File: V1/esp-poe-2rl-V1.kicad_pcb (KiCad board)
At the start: 4 copper layers, 88 x 45 mm, 100 parts, among them J1 USB_C_Receptacle_USB2.0, J2 1x2P 5,08mm, J3 1x2P 5,08mm, J4 RJ45 JACK, K1 G5NB-1A-E-DC5, K2 G5NB-1A-E-DC5, Q1 WPM2015-3/TR, Q2 LMUN2211LT1G, Q3 UMH3N, Q4 MMBT2222A, Q5 MMBT2222A, SW1 RESET, U1 CH340K, U2 ESP32-WROOM-32UE-N16, U3 LAN8710A, U4 TX4138, U5 SY8089A1AAC, U6 TPS2376DDAR-H

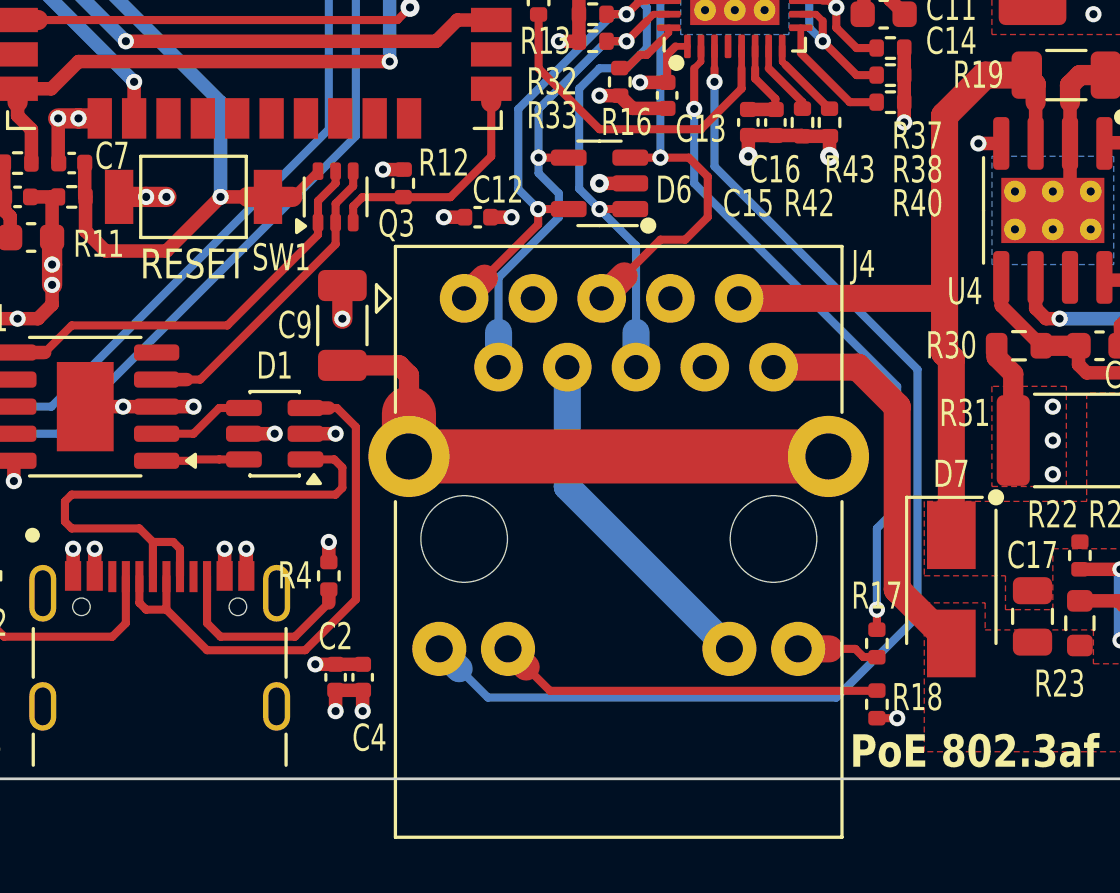
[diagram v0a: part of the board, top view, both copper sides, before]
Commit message: Update power rail names
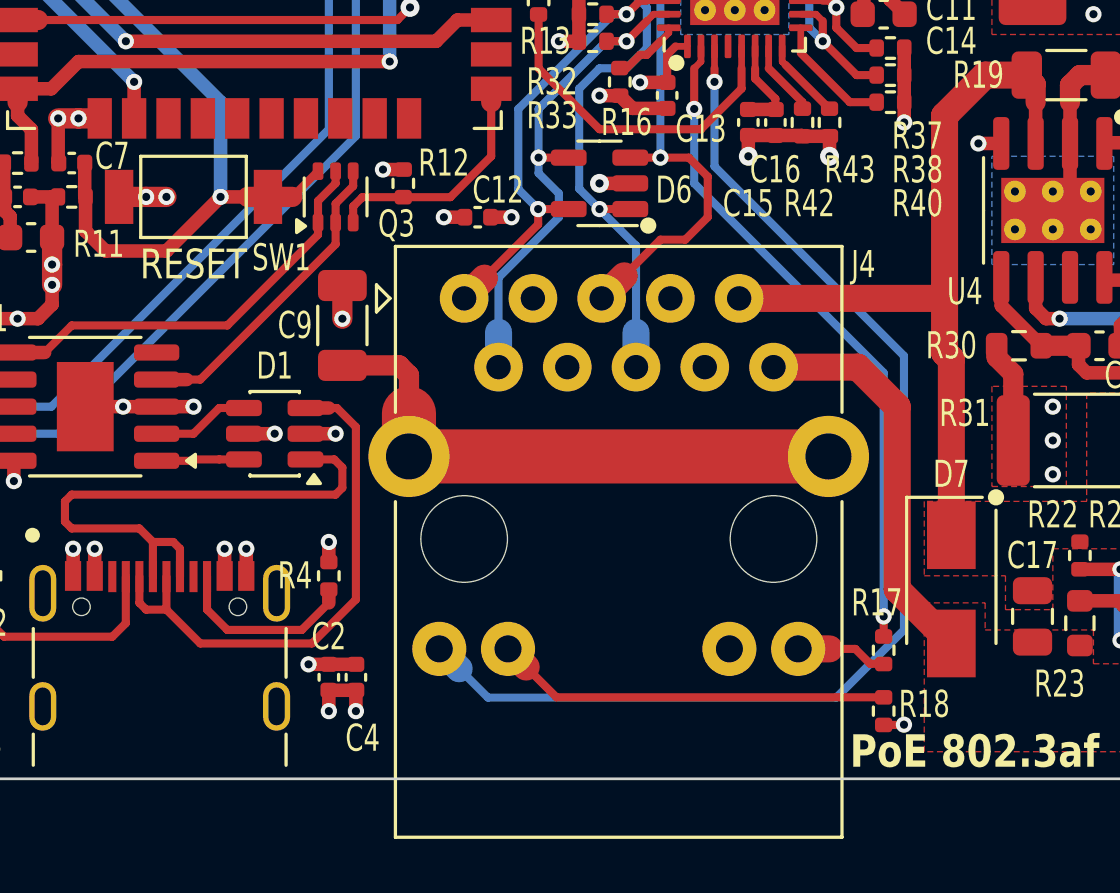
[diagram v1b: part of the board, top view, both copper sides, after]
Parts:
- moved R17 0.35 mm to (137.5, 111.2)
- moved R18 0.35 mm to (137.5, 113.5)
- moved C2 0.25 mm to (117.0, 112.2)
- moved C4 0.25 mm to (118.0, 112.2)
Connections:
- J4 pad 13: +3V3A -> +3V3LAN
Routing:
- net +3V3LAN: track 13.4 -> 36.8 mm
- net +3V3A: track 27.8 -> 14.9 mm
- net 5VUSB: track 88.9 -> 96.8 mm
- net /USBCC2: track 7.43 -> 6.93 mm

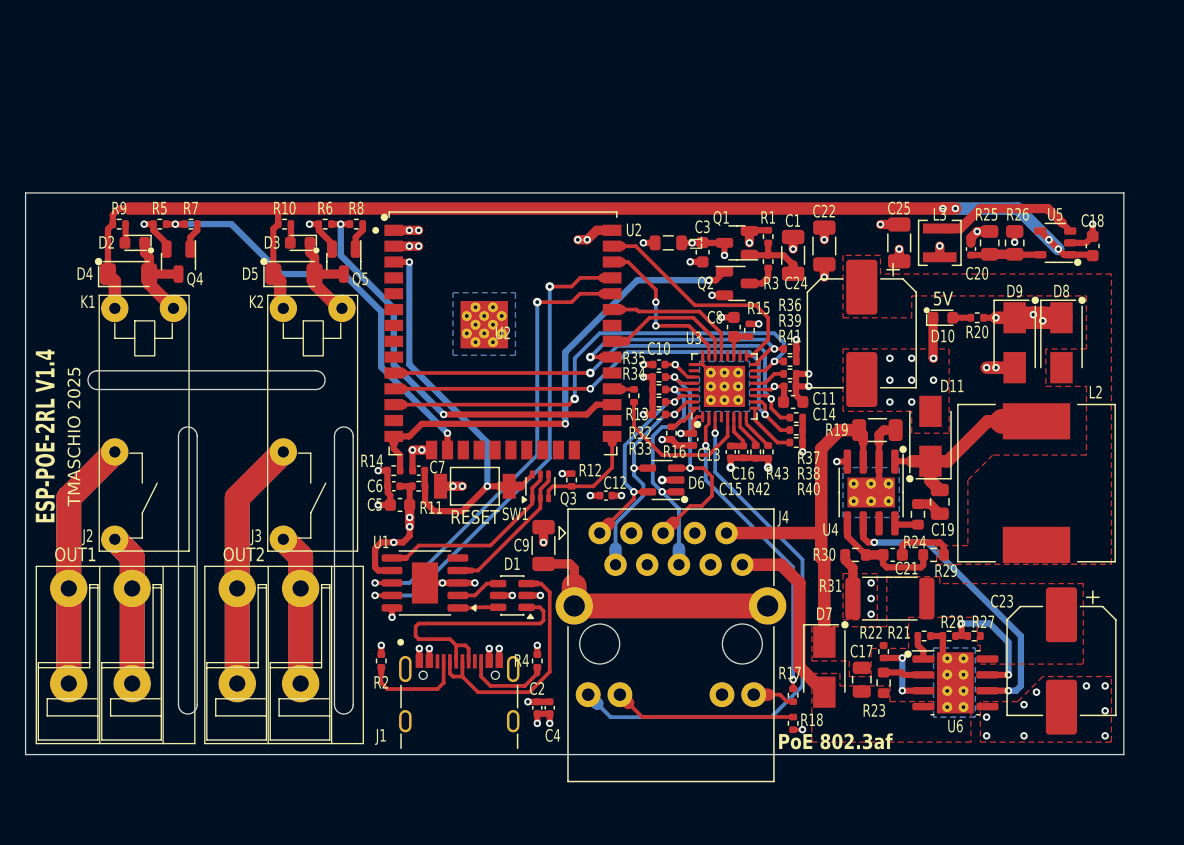
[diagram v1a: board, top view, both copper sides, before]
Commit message: addressing the PHY power rails
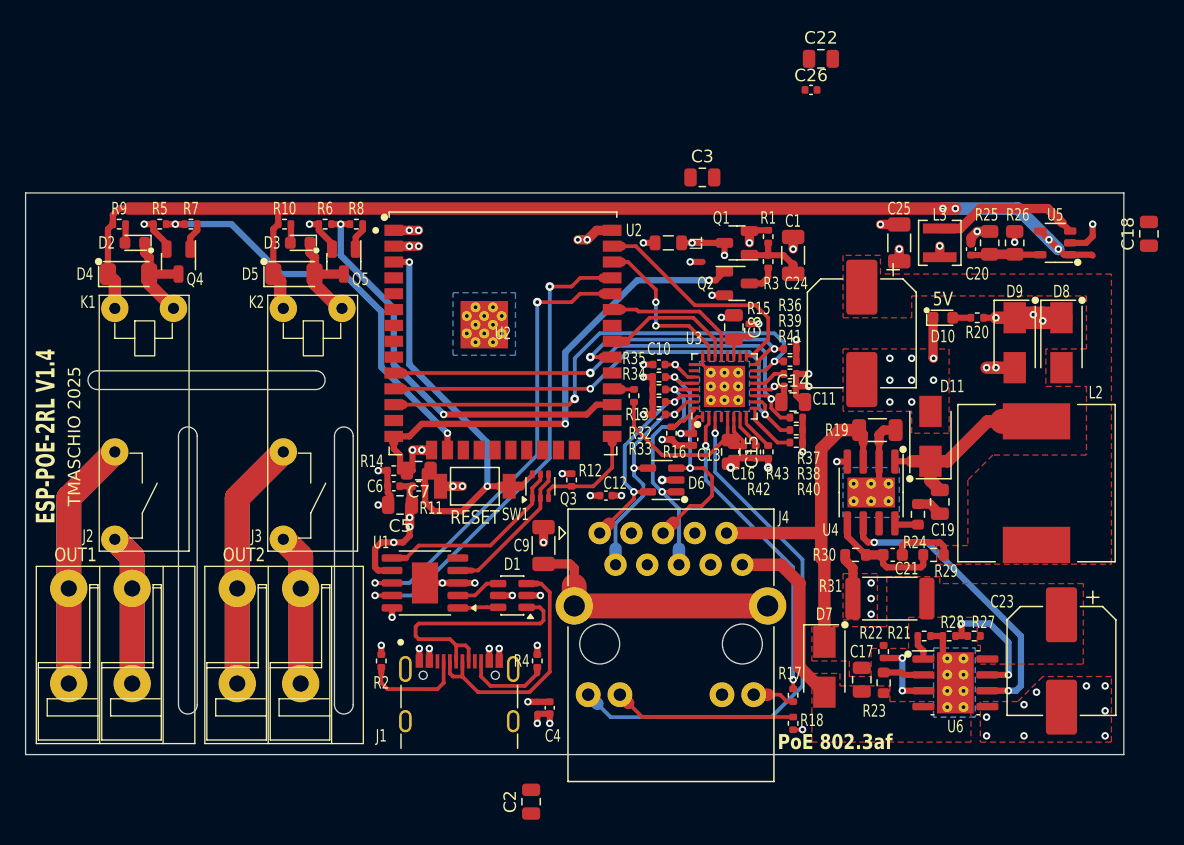
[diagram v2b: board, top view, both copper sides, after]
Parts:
- added C26: 100nF/50V, Tales:C_0402_1005Metric, F.Cu at (138.9, 62.7)
- C14, C18, C3, C5, C8: value 10uF/10V -> 10uF/25V; footprint Tales:C_0603_1608Metric -> Tales:C_0805_2012Metric
- C15, C2, C7: value 1uF/25V -> 1uF/50V; footprint Tales:C_0402_1005Metric -> Tales:C_0805_2012Metric
- C22: value 22uF/10V -> 10uF/25V; footprint Tales:C_1206_3216Metric -> Tales:C_0805_2012Metric
- R13: value 22R -> 33R
- moved C22 15.0 mm to (139.7, 60.3), turned to 0 degrees
- moved C2 7.54 mm to (116.5, 119.8), turned to 90 degrees
- moved C3 6.00 mm to (130.2, 69.8), turned to 0 degrees
- moved C18 4.61 mm to (166.0, 74.3)
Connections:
- net /EMACGPIO renamed /ESPCLK
- J4 pad 11: /ETHLEDY -> /ETHLEDYA
- J4 pad 12: /ETHLEDYK -> GND
- J4 pad 13: +3V3LAN -> /ETHLEDGA
- R17 pad 1: /ETHLEDGK -> /ETHLEDGA
- R17 pad 2: /ETHLEDG -> +3V3LAN
- R18 pad 1: /ETHLEDYK -> /ETHLEDYA
- R18 pad 2: GND -> /ETHLEDY
- U3 pad 2: /ETHLEDG -> /ETHLEDGK
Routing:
- net /ETHLEDG: track 24.8 -> 0.00 mm, vias 2 -> 0
- net (no net): track 0.00 -> 24.8 mm
- net /ETHLEDYK: track 14.6 -> 0.00 mm
- net GND: track 69.5 -> 82.4 mm, vias 59 -> 58
- net +3V3: track 36.8 -> 35.8 mm, vias 13 -> 12
- net /ETHLEDY: track 43.4 -> 44.2 mm
- net /ETHLEDGK: vias 0 -> 2

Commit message: Update esp-poe-2rl-V1.kicad_pcb
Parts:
- moved R18 23.5 mm to (118.2, 100.0), turned to 90 degrees
- moved C9 14.2 mm to (117.5, 113.5), turned to -90 degrees
- moved R17 11.3 mm to (137.2, 100.0)
- moved C4 7.50 mm to (113.5, 106.2), turned to 0 degrees
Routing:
- net 5VUSB: track 96.8 -> 24.3 mm, vias 6 -> 5
- net /ETHLEDY: track 44.2 -> 4.44 mm
- net (no net): track 24.8 -> 0.00 mm
- net +3V3LAN: track 36.8 -> 13.4 mm
- net GND: track 82.4 -> 64.2 mm, vias 58 -> 53
- net /ETHSH: track 21.1 -> 15.5 mm
- net POE+: track 29.5 -> 33.0 mm, vias 0 -> 3
- net POE-: track 17.7 -> 20.4 mm, vias 0 -> 3
- net /ETHLEDGK: track 3.39 -> 5.17 mm, vias 2 -> 1

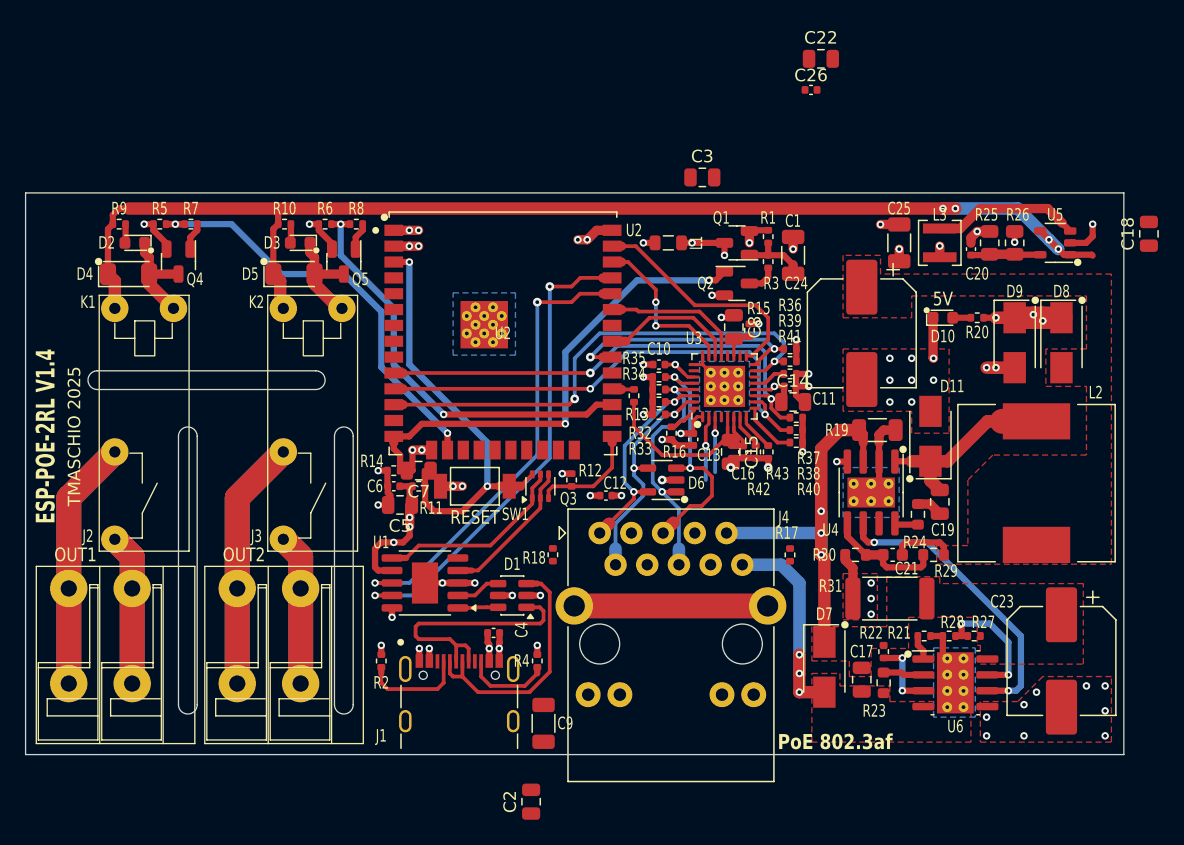
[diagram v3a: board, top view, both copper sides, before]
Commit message: Replaced terminal blocks
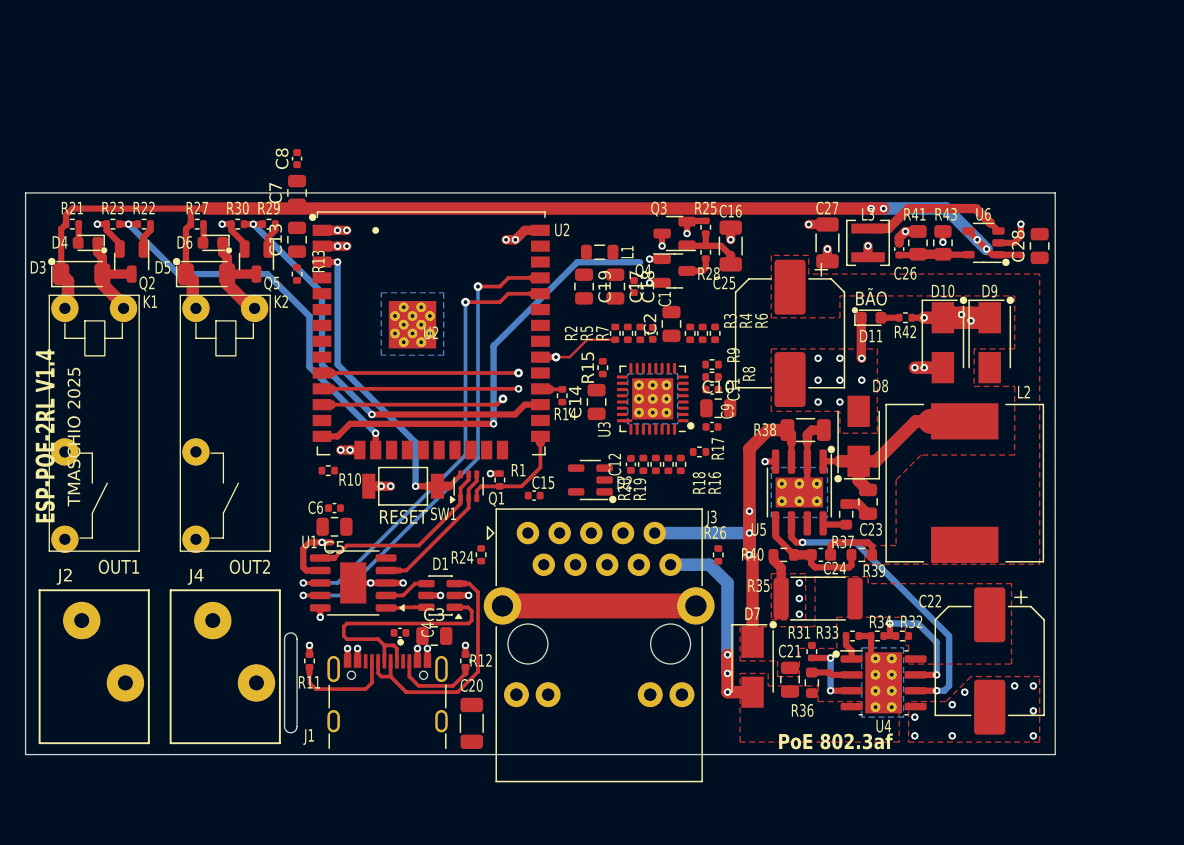
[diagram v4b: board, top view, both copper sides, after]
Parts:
- removed the C22 at (139.7, 60.3)
- removed the J3 at (95.5, 106.5)
- added C18: 100nF/50V, Tales:C_0402_1005Metric, F.Cu at (124.8, 78.5)
- added C19: 10uF/25V, Tales:C_0805_2012Metric, F.Cu at (120.8, 78.5)
- added C7: 10uF/25V, Tales:C_0805_2012Metric, F.Cu at (97.8, 71.0)
- added J4: 250-202, Tales:TerminalBlock_Wago_250-202_1x02_P3.5mm_45Degree, F.Cu at (92.8, 107.8)
- J2: value 1x2P 5,08mm -> 250-202; footprint Tales:TerminalBlock_Dibo_DB142R-5.08-2P_1x02_P5.08mm_Horizontal -> Tales:TerminalBlock_Wago_250-202_1x02_P3.5mm_45Degree
- R2: renamed from R36; value 2k2 -> 10k
- R3: renamed from R37; value 2k2 -> 10k
- R4: renamed from R38; value 2k2 -> 10k
- R5: renamed from R39; value 2k2 -> 10k
- R6: renamed from R40; value 2k2 -> 10k
- R7: renamed from R41; value 2k2 -> 10k
- R8: renamed from R42; value 2k2 -> 10k
- R9: renamed from R43; value 2k2 -> 10k
- moved C8 41.6 mm to (97.8, 68.2), turned to 90 degrees
- moved C13 20.9 mm to (97.8, 74.8), turned to 90 degrees
- moved R13 19.6 mm to (97.8, 77.5), turned to 90 degrees
- moved C3 15.4 mm to (108.8, 106.5), turned to 0 degrees
- moved R2 14.1 mm to (123.2, 82.2), turned to -90 degrees
- moved R5 13.2 mm to (124.2, 82.2), turned to -90 degrees
- moved C14 12.5 mm to (121.8, 87.8), turned to 90 degrees
- moved R7 12.4 mm to (125.2, 82.2), turned to -90 degrees
- moved R15 12.1 mm to (122.2, 85.0)
- moved C1 11.8 mm to (126.2, 82.2), turned to 90 degrees
- moved C2 11.6 mm to (127.8, 81.5), turned to 90 degrees
- moved C17 11.2 mm to (123.2, 78.5), turned to -90 degrees
- moved R6 10.9 mm to (131.2, 82.2), turned to -90 degrees
- moved R3 10.9 mm to (129.2, 82.2), turned to -90 degrees
- moved R4 10.8 mm to (130.2, 82.2), turned to -90 degrees
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- renumbered C11 to C1, C15 to C10, C16 to C11, C10 to C12, C7 to C13, C8 to C14, C12 to C15, C1 to C16, C3 to C17, C14 to C2, C9 to C20, C17 to C21, C23 to C22, C19 to C23, C21 to C24, C24 to C25, C20 to C26, C25 to C27, C18 to C28, C2 to C3, C26 to C8, C13 to C9, D9 to D10, D10 to D11, D6 to D2, D4 to D3, D2 to D4, D3 to D6, D11 to D8, D8 to D9, J4 to J3, Q3 to Q1, Q4 to Q2, Q1 to Q3, Q2 to Q4, R12 to R1, R14 to R10, R2 to R11, R4 to R12, R11 to R13, R13 to R14, R33 to R16, R16 to R17, R32 to R18, R34 to R19, R35 to R20, R9 to R21, R7 to R22, R5 to R23, R18 to R24, R1 to R25, R17 to R26, R10 to R27, R3 to R28, R8 to R29, R6 to R30, R22 to R31, R27 to R32, R21 to R33, R28 to R34, R31 to R35, R23 to R36, R24 to R37, R19 to R38, R29 to R39, R30 to R40, R25 to R41, R20 to R42, R26 to R43, U6 to U4, U4 to U5, U5 to U6
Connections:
- J3 pad 11: /ETHLEDYA -> +3V3LAN
- J3 pad 12: GND -> /ETHLEDYK
- R24 pad 1: /ETHLEDYA -> /ETHLEDYK
- R26 pad 1: /ETHLEDGA -> GND
- R26 pad 2: +3V3LAN -> /ETHLEDGK
- U3 pad 2: /ETHLEDGK -> /ETHLEDY
- U3 pad 3: /ETHLEDY -> /ETHLEDGA
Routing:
- net /OUT2LN: track 40.2 -> 0.00 mm
- net /OUT1LN: track 40.2 -> 0.00 mm
- net GND: track 64.2 -> 38.2 mm, vias 53 -> 42
- net /EMACRX: track 40.3 -> 14.7 mm, vias 2 -> 1
- net /OUT2LD: track 24.3 -> 0.00 mm
- net /OUT1LD: track 24.3 -> 0.00 mm
- net /EMACRXD1: track 39.4 -> 15.8 mm, vias 2 -> 1
- net /EMACRXD0: track 38.8 -> 15.8 mm, vias 2 -> 1
- net /ETHTXD+: track 20.3 -> 0.00 mm, vias 2 -> 0
- net /ETHTXD-: track 20.1 -> 0.00 mm, vias 2 -> 0
- net /ETHRXD+: track 19.2 -> 0.00 mm, vias 2 -> 0
- net /EMACMDC: track 18.9 -> 0.00 mm
- net /ETHRXD-: track 17.5 -> 0.00 mm, vias 2 -> 0
- net +5V: track 117.8 -> 103.8 mm
- net /EMACMDIO: track 20.2 -> 6.58 mm, vias 2 -> 1
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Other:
- board size 88 x 45 mm -> 82.5 x 45 mm
- board text added: "BÃO"
- board text removed: "5V"

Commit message: V1.5.0
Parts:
- added G***: LOGO, Tales:Eumesmo_small_silk, F.Cu at (148.3, 76.3)
- added G***: LOGO, Tales:Eumesmo_small_silk, F.Cu at (136.2, 74.5)
- L2: footprint Tales:L_12x12mm_h6mm -> Tales:L_12x12mm_H6mm
- L3: footprint Tales:L_3x3mm_h1.5mm -> Tales:L_3x3mm_H1.5mm
- moved D2 9.01 mm to (130.2, 93.5), turned to 0 degrees
- moved R16 7.20 mm to (121.8, 95.2), turned to 180 degrees
- moved C8 7.16 mm to (96.2, 75.2)
- moved R18 5.84 mm to (121.8, 93.8), turned to 180 degrees
- moved R19 4.75 mm to (121.8, 92.8), turned to 180 degrees
- moved R20 3.88 mm to (121.8, 91.8), turned to 180 degrees
- moved C7 3.75 mm to (97.8, 74.8)
- moved C13 3.50 mm to (97.8, 78.2), turned to -90 degrees
- moved R3 2.51 mm to (126.8, 82.0)
- moved R4 2.51 mm to (127.8, 82.0)
- moved R6 2.51 mm to (128.8, 82.0)
- moved C1 2.50 mm to (123.8, 82.2)
- moved C2 2.50 mm to (125.2, 81.5)
- moved R2 2.50 mm to (120.8, 82.2)
- moved R5 2.50 mm to (121.8, 82.2)
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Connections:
- D2 pad 3: /ETHTXD- -> /ETHRXD-
- D2 pad 5: /ETHRXD- -> /ETHTXD-
- J3 pad 11: +3V3LAN -> +3V3A
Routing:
- net 5VUSB: track 23.0 -> 73.8 mm
- net +3V3A: track 3.07 -> 48.6 mm, vias 0 -> 7
- net /ETHLEDY: track 0.00 -> 36.4 mm
- net GND: track 38.2 -> 71.6 mm, vias 42 -> 52
- net /ETHLEDGA: track 0.00 -> 31.0 mm
- net /EMACTXD1: track 0.00 -> 30.1 mm, vias 0 -> 2
- net /EMACTXD0: track 0.00 -> 30.0 mm, vias 0 -> 2
- net /EMACTXEN: track 0.00 -> 30.0 mm, vias 0 -> 2
- net /EMACCLK: track 0.00 -> 29.6 mm
- net /ETHRXD+: track 0.00 -> 24.7 mm
- net /EMACMDC: track 0.00 -> 21.8 mm, vias 0 -> 2
- net /ETHRXD-: track 0.00 -> 21.7 mm, vias 0 -> 2
- net /ETHTXD+: track 0.00 -> 20.8 mm, vias 0 -> 2
- net /ETHTXD-: track 0.00 -> 20.4 mm, vias 0 -> 2
- net +3V3LAN: track 1.00 -> 19.9 mm, vias 1 -> 5
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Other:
- outline, holes or cut-outs redrawn
- board text added: "5V"
- board text added: "ESP-POE-2RL V1.5"
- board text added: "V1.5.0 2026-06-08"
- board text removed: "BÃO"
- board text removed: "ESP-POE-2RL V1.4"
- board text removed: "TMASCHIO 2025"
